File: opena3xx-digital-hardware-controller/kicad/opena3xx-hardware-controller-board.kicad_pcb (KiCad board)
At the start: 2 copper layers, 156.3 x 80.6 mm, 52 parts, among them J1 Conn_02x01, J2 Conn_02x01, J3 Conn_02x01, J4 Conn_02x01, J5 Raspberry_Pi_Zero, SW1 SW_MEC_5E, U1 MCP23017_SO, U2 MCP23017_SO, U3 MCP23017_SO, U4 MCP23017_SO, U5 MCP23017_SO, U6 MCP23017_SO, U7 MCP23017_SO, U8 MCP23017_SO

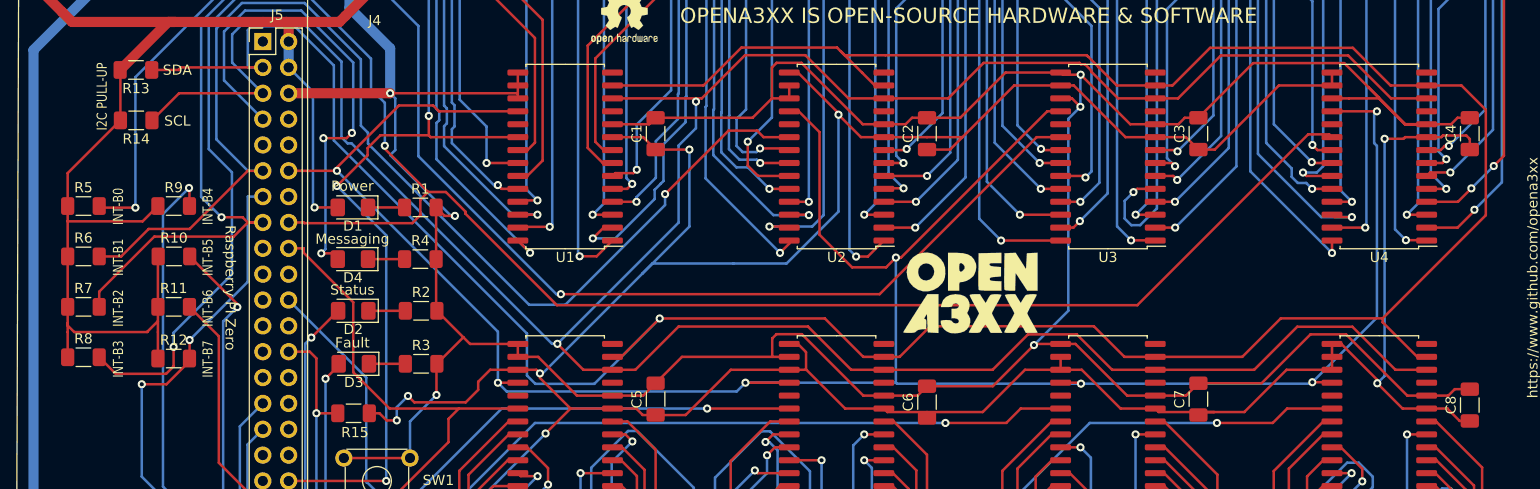
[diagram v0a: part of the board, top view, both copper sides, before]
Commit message: Changed text from Messaging to Signal in Top Mask
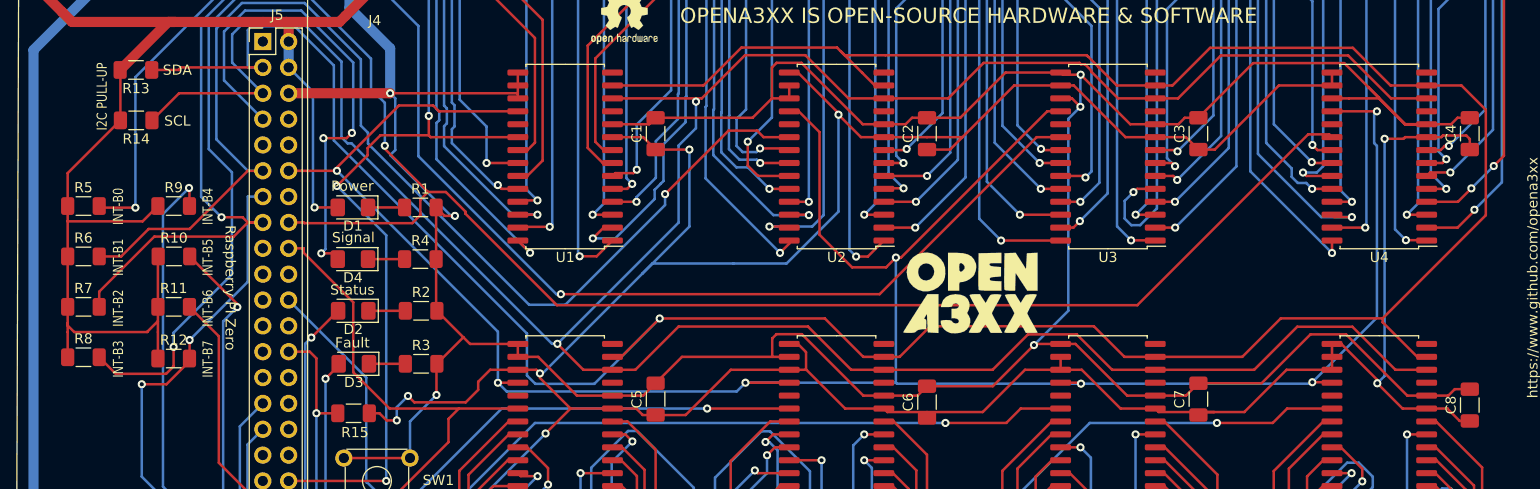
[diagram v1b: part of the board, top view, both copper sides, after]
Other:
- board text added: "Signal"
- board text removed: "Messaging"

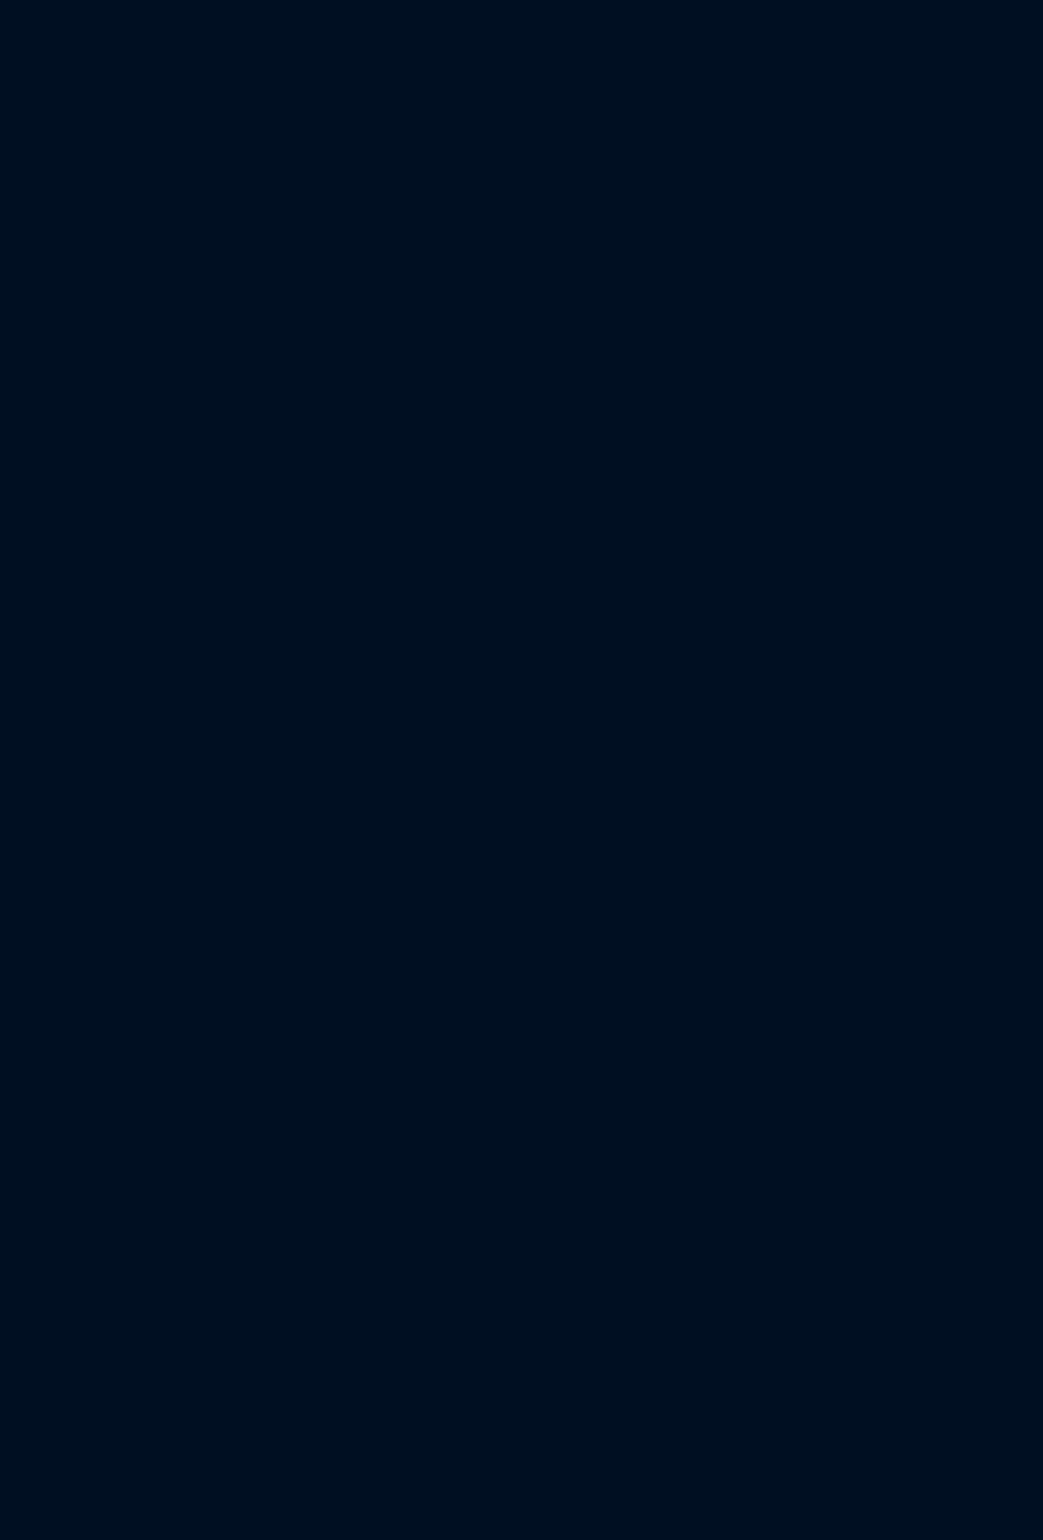
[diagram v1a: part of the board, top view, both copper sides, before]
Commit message: Created mcdu project in Kicad
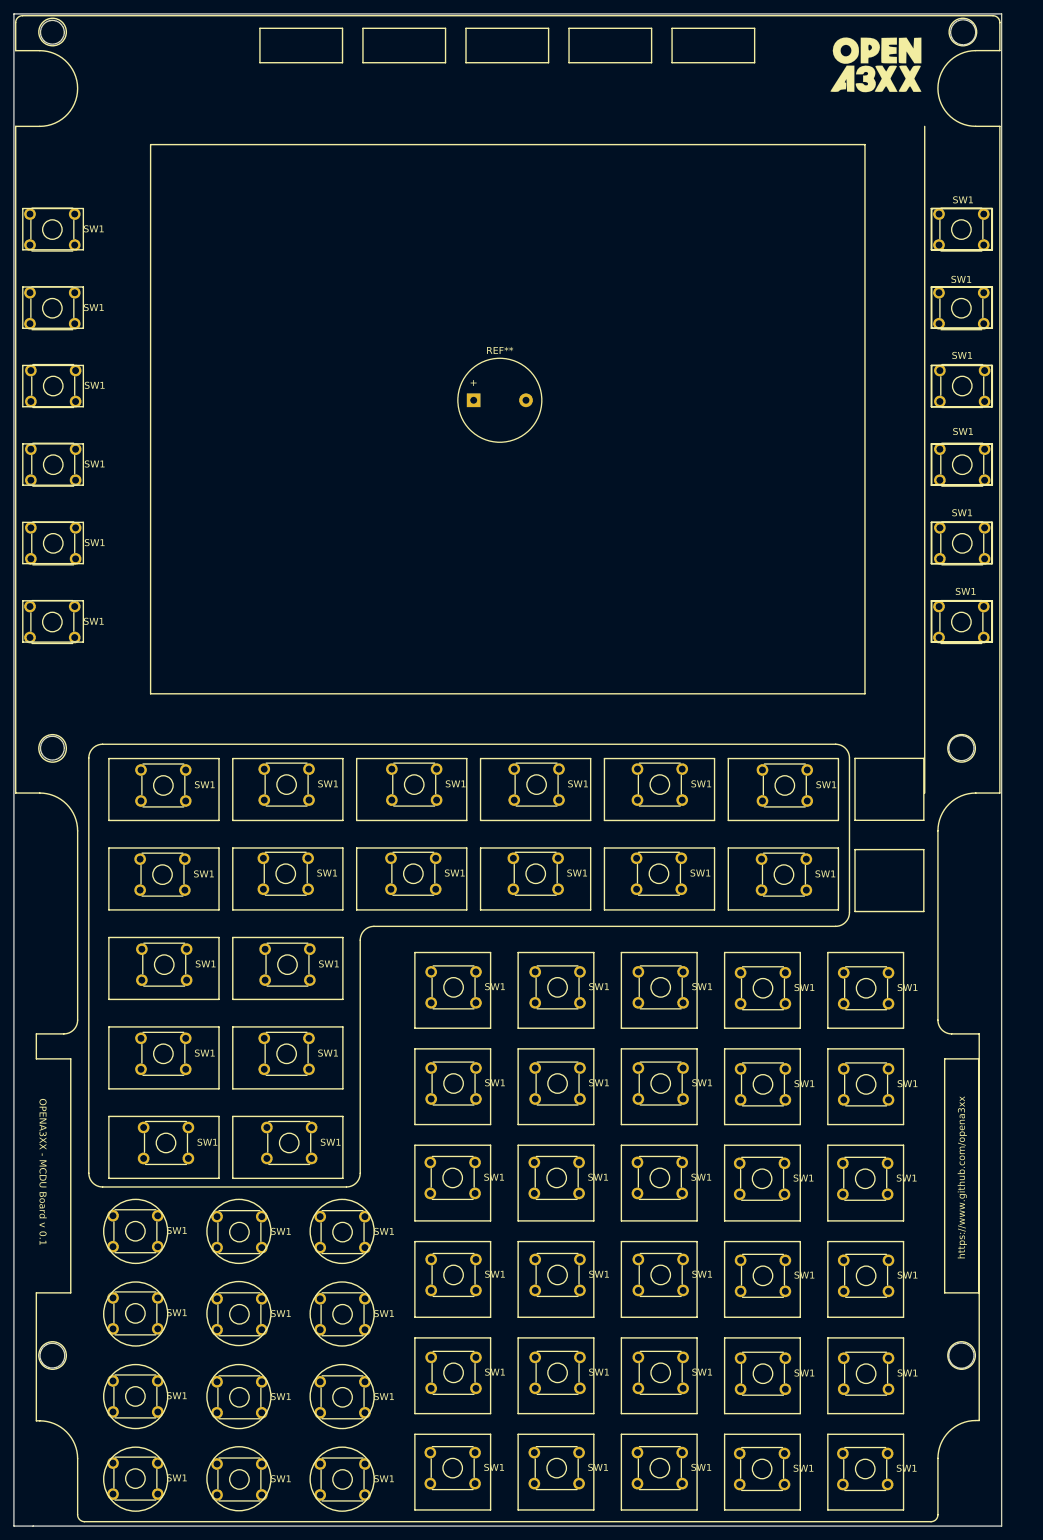
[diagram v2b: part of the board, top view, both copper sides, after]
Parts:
- added G***: LOGO, openaa3xx:logo_180x112, F.Cu at (-34.2, -0.78)
- added REF**: Buzzer_12x9.5RM7.6, Buzzer_Beeper:Buzzer_12x9.5RM7.6, F.Cu at (-92.4, 47.9)
- added SW1: SW_MEC_5E, Button_Switch_THT:SW_TH_Tactile_Omron_B3F-10xx, F.Cu at (-122.5, 153.6)
- added SW1: SW_MEC_5E, Button_Switch_THT:SW_TH_Tactile_Omron_B3F-10xx, F.Cu at (-68.6, 101.5)
- added SW1: SW_MEC_5E, Button_Switch_THT:SW_TH_Tactile_Omron_B3F-10xx, F.Cu at (-86.6, 114.5)
- added SW1: SW_MEC_5E, Button_Switch_THT:SW_TH_Tactile_Omron_B3F-10xx, F.Cu at (-86.5, 101.5)
- added SW1: SW_MEC_5E, Button_Switch_THT:SW_TH_Tactile_Omron_B3F-10xx, F.Cu at (-104.4, 114.5)
- added SW1: SW_MEC_5E, Button_Switch_THT:SW_TH_Tactile_Omron_B3F-10xx, F.Cu at (-104.3, 101.5)
- added SW1: SW_MEC_5E, Button_Switch_THT:SW_TH_Tactile_Omron_B3F-10xx, F.Cu at (-123.0, 114.5)
- added SW1: SW_MEC_5E, Button_Switch_THT:SW_TH_Tactile_Omron_B3F-10xx, F.Cu at (-122.8, 101.5)
- added SW1: SW_MEC_5E, Button_Switch_THT:SW_TH_Tactile_Omron_B3F-10xx, F.Cu at (-140.9, 114.6)
- added SW1: SW_MEC_5E, Button_Switch_THT:SW_TH_Tactile_Omron_B3F-10xx, F.Cu at (-140.7, 101.6)
- added SW1: SW_MEC_5E, Button_Switch_THT:SW_TH_Tactile_Omron_B3F-10xx, F.Cu at (-98.7, 200.8)
- added SW1: SW_MEC_5E, Button_Switch_THT:SW_TH_Tactile_Omron_B3F-10xx, F.Cu at (-140.4, 153.6)
- added SW1: SW_MEC_5E, Button_Switch_THT:SW_TH_Tactile_Omron_B3F-10xx, F.Cu at (-53.7, 201.0)
- added SW1: SW_MEC_5E, Button_Switch_THT:SW_TH_Tactile_Omron_B3F-10xx, F.Cu at (-83.6, 200.8)
- added SW1: SW_MEC_5E, Button_Switch_THT:SW_TH_Tactile_Omron_B3F-10xx, F.Cu at (-38.8, 201.0)
- added SW1: SW_MEC_5E, Button_Switch_THT:SW_TH_Tactile_Omron_B3F-10xx, F.Cu at (-68.6, 200.8)
- added SW1: SW_MEC_5E, Button_Switch_THT:SW_TH_Tactile_Omron_B3F-10xx, F.Cu at (-98.6, 187.0)
- added SW1: SW_MEC_5E, Button_Switch_THT:SW_TH_Tactile_Omron_B3F-10xx, F.Cu at (-53.6, 187.1)
- added SW1: SW_MEC_5E, Button_Switch_THT:SW_TH_Tactile_Omron_B3F-10xx, F.Cu at (-83.5, 187.0)
- added SW1: SW_MEC_5E, Button_Switch_THT:SW_TH_Tactile_Omron_B3F-10xx, F.Cu at (-38.6, 187.1)
- added SW1: SW_MEC_5E, Button_Switch_THT:SW_TH_Tactile_Omron_B3F-10xx, F.Cu at (-68.5, 187.0)
- added SW1: SW_MEC_5E, Button_Switch_THT:SW_TH_Tactile_Omron_B3F-10xx, F.Cu at (-98.6, 172.8)
- added SW1: SW_MEC_5E, Button_Switch_THT:SW_TH_Tactile_Omron_B3F-10xx, F.Cu at (-122.8, 140.6)
- added SW1: SW_MEC_5E, Button_Switch_THT:SW_TH_Tactile_Omron_B3F-10xx, F.Cu at (-53.6, 172.9)
- added SW1: SW_MEC_5E, Button_Switch_THT:SW_TH_Tactile_Omron_B3F-10xx, F.Cu at (-83.5, 172.8)
- added SW1: SW_MEC_5E, Button_Switch_THT:SW_TH_Tactile_Omron_B3F-10xx, F.Cu at (-38.6, 172.9)
- added SW1: SW_MEC_5E, Button_Switch_THT:SW_TH_Tactile_Omron_B3F-10xx, F.Cu at (-68.5, 172.8)
- added SW1: SW_MEC_5E, Button_Switch_THT:SW_TH_Tactile_Omron_B3F-10xx, F.Cu at (-98.7, 158.7)
- added SW1: SW_MEC_5E, Button_Switch_THT:SW_TH_Tactile_Omron_B3F-10xx, F.Cu at (-53.7, 158.8)
- added SW1: SW_MEC_5E, Button_Switch_THT:SW_TH_Tactile_Omron_B3F-10xx, F.Cu at (-83.6, 158.7)
- added SW1: SW_MEC_5E, Button_Switch_THT:SW_TH_Tactile_Omron_B3F-10xx, F.Cu at (-38.8, 158.8)
- added SW1: SW_MEC_5E, Button_Switch_THT:SW_TH_Tactile_Omron_B3F-10xx, F.Cu at (-68.6, 158.7)
- added SW1: SW_MEC_5E, Button_Switch_THT:SW_TH_Tactile_Omron_B3F-10xx, F.Cu at (-98.6, 144.9)
- added SW1: SW_MEC_5E, Button_Switch_THT:SW_TH_Tactile_Omron_B3F-10xx, F.Cu at (-122.7, 127.7)
- added SW1: SW_MEC_5E, Button_Switch_THT:SW_TH_Tactile_Omron_B3F-10xx, F.Cu at (-53.6, 145.1)
- added SW1: SW_MEC_5E, Button_Switch_THT:SW_TH_Tactile_Omron_B3F-10xx, F.Cu at (-83.5, 144.9)
- added SW1: SW_MEC_5E, Button_Switch_THT:SW_TH_Tactile_Omron_B3F-10xx, F.Cu at (-38.6, 145.1)
- added SW1: SW_MEC_5E, Button_Switch_THT:SW_TH_Tactile_Omron_B3F-10xx, F.Cu at (-68.5, 144.9)
- added SW1: SW_MEC_5E, Button_Switch_THT:SW_TH_Tactile_Omron_B3F-10xx, F.Cu at (-38.6, 131.1)
- added SW1: SW_MEC_5E, Button_Switch_THT:SW_TH_Tactile_Omron_B3F-10xx, F.Cu at (-53.6, 131.1)
- added SW1: SW_MEC_5E, Button_Switch_THT:SW_TH_Tactile_Omron_B3F-10xx, F.Cu at (-68.5, 131.0)
- added SW1: SW_MEC_5E, Button_Switch_THT:SW_TH_Tactile_Omron_B3F-10xx, F.Cu at (-83.5, 131.0)
- added SW1: SW_MEC_5E, Button_Switch_THT:SW_TH_Tactile_Omron_B3F-10xx, F.Cu at (-98.6, 131.0)
- added SW1: SW_MEC_5E, Button_Switch_THT:SW_TH_Tactile_Omron_B3F-10xx, F.Cu at (-114.7, 202.5)
- added SW1: SW_MEC_5E, Button_Switch_THT:SW_TH_Tactile_Omron_B3F-10xx, F.Cu at (-140.7, 140.6)
- added SW1: SW_MEC_5E, Button_Switch_THT:SW_TH_Tactile_Omron_B3F-10xx, F.Cu at (-144.8, 202.3)
- added SW1: SW_MEC_5E, Button_Switch_THT:SW_TH_Tactile_Omron_B3F-10xx, F.Cu at (-129.7, 202.5)
- added SW1: SW_MEC_5E, Button_Switch_THT:SW_TH_Tactile_Omron_B3F-10xx, F.Cu at (-114.7, 190.5)
- added SW1: SW_MEC_5E, Button_Switch_THT:SW_TH_Tactile_Omron_B3F-10xx, F.Cu at (-144.8, 190.4)
- added SW1: SW_MEC_5E, Button_Switch_THT:SW_TH_Tactile_Omron_B3F-10xx, F.Cu at (-129.7, 190.5)
- added SW1: SW_MEC_5E, Button_Switch_THT:SW_TH_Tactile_Omron_B3F-10xx, F.Cu at (-114.7, 178.5)
- added SW1: SW_MEC_5E, Button_Switch_THT:SW_TH_Tactile_Omron_B3F-10xx, F.Cu at (-144.8, 178.3)
- added SW1: SW_MEC_5E, Button_Switch_THT:SW_TH_Tactile_Omron_B3F-10xx, F.Cu at (-129.7, 178.5)
- added SW1: SW_MEC_5E, Button_Switch_THT:SW_TH_Tactile_Omron_B3F-10xx, F.Cu at (-114.7, 166.5)
- added SW1: SW_MEC_5E, Button_Switch_THT:SW_TH_Tactile_Omron_B3F-10xx, F.Cu at (-24.7, 43.6)
- added SW1: SW_MEC_5E, Button_Switch_THT:SW_TH_Tactile_Omron_B3F-10xx, F.Cu at (-140.6, 127.7)
- added SW1: SW_MEC_5E, Button_Switch_THT:SW_TH_Tactile_Omron_B3F-10xx, F.Cu at (-24.8, 20.9)
- added SW1: SW_MEC_5E, Button_Switch_THT:SW_TH_Tactile_Omron_B3F-10xx, F.Cu at (-24.8, 77.9)
- added SW1: SW_MEC_5E, Button_Switch_THT:SW_TH_Tactile_Omron_B3F-10xx, F.Cu at (-24.7, 66.5)
- added SW1: SW_MEC_5E, Button_Switch_THT:SW_TH_Tactile_Omron_B3F-10xx, F.Cu at (-24.7, 55.0)
- added SW1: SW_MEC_5E, Button_Switch_THT:SW_TH_Tactile_Omron_B3F-10xx, F.Cu at (-24.8, 32.3)
- added SW1: SW_MEC_5E, Button_Switch_THT:SW_TH_Tactile_Omron_B3F-10xx, F.Cu at (-129.7, 166.5)
- added SW1: SW_MEC_5E, Button_Switch_THT:SW_TH_Tactile_Omron_B3F-10xx, F.Cu at (-144.8, 166.4)
- added SW1: SW_MEC_5E, Button_Switch_THT:SW_TH_Tactile_Omron_B3F-10xx, F.Cu at (-156.9, 77.9)
- added SW1: SW_MEC_5E, Button_Switch_THT:SW_TH_Tactile_Omron_B3F-10xx, F.Cu at (-156.7, 66.5)
- added SW1: SW_MEC_5E, Button_Switch_THT:SW_TH_Tactile_Omron_B3F-10xx, F.Cu at (-156.7, 55.0)
- added SW1: SW_MEC_5E, Button_Switch_THT:SW_TH_Tactile_Omron_B3F-10xx, F.Cu at (-50.6, 114.6)
- added SW1: SW_MEC_5E, Button_Switch_THT:SW_TH_Tactile_Omron_B3F-10xx, F.Cu at (-156.7, 43.6)
- added SW1: SW_MEC_5E, Button_Switch_THT:SW_TH_Tactile_Omron_B3F-10xx, F.Cu at (-156.9, 32.3)
- added SW1: SW_MEC_5E, Button_Switch_THT:SW_TH_Tactile_Omron_B3F-10xx, F.Cu at (-156.9, 20.9)
- added SW1: SW_MEC_5E, Button_Switch_THT:SW_TH_Tactile_Omron_B3F-10xx, F.Cu at (-50.4, 101.6)
- added SW1: SW_MEC_5E, Button_Switch_THT:SW_TH_Tactile_Omron_B3F-10xx, F.Cu at (-68.7, 114.5)
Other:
- board size 156.3 x 80.6 mm -> 374.5 x 219.7 mm
- board text added: "OPENA3XX - MCDU Board v 0.1"

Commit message: WIP Schematic & PCB for the MCDU Added custom Kicad Packages for the Tactile Switchs (LED EMBEDDED)
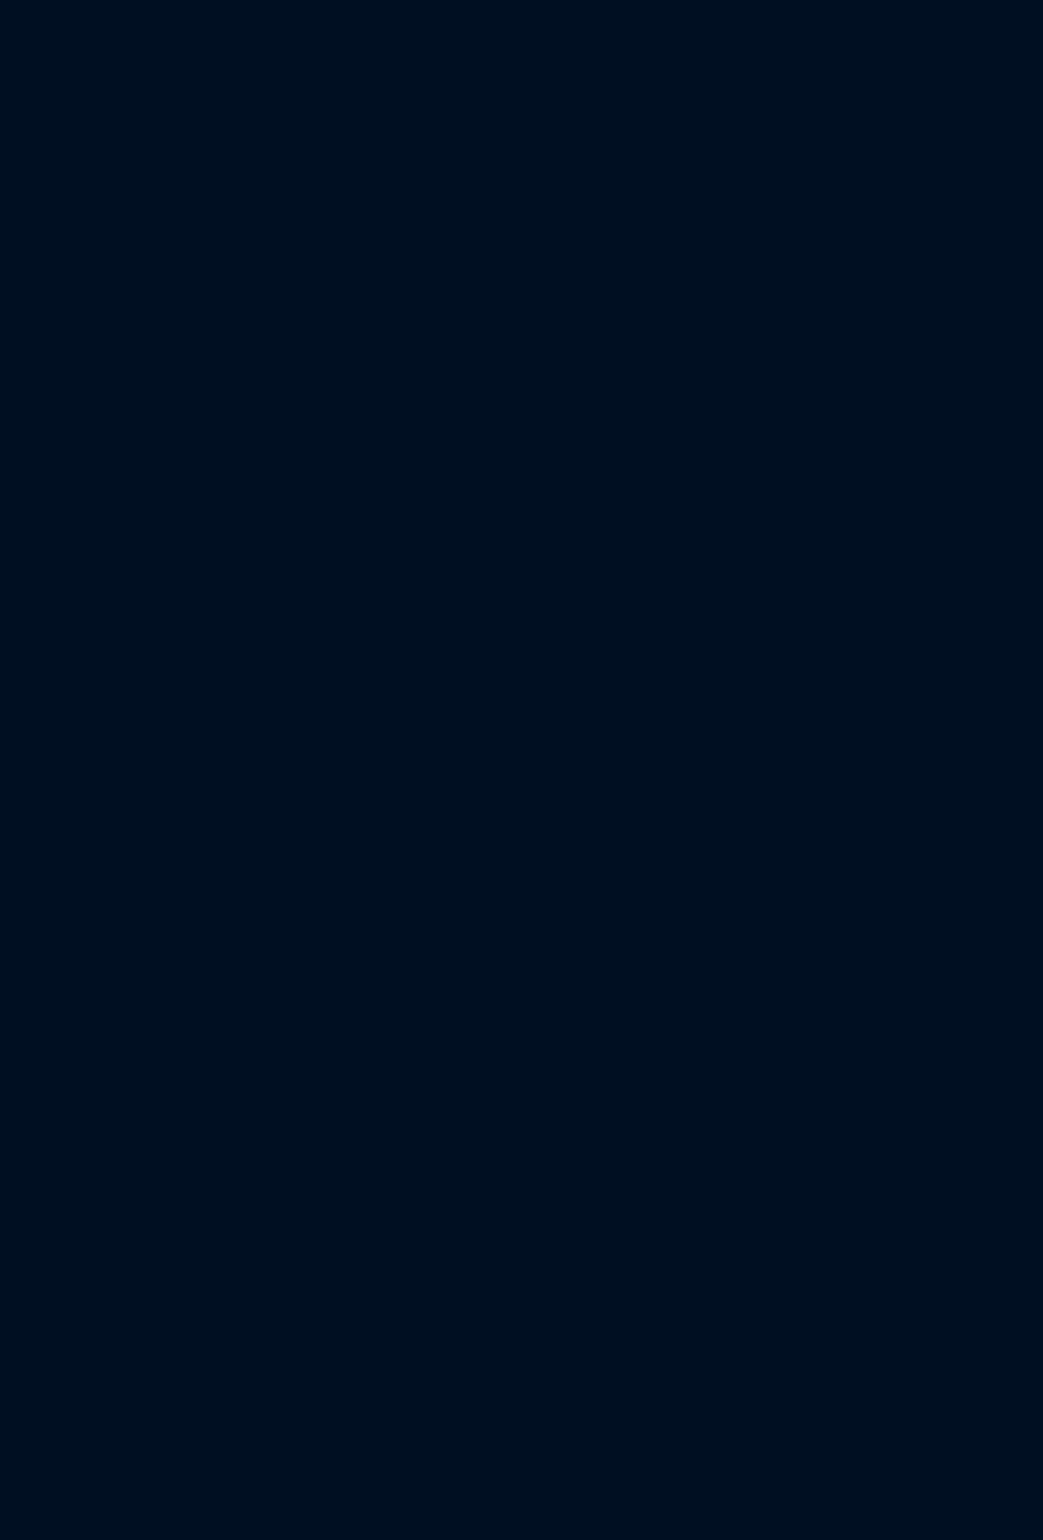
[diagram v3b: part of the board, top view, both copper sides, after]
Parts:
- removed the G*** at (-34.2, -0.78)
- removed the REF** at (-92.4, 47.9)
- removed the SW1 at (-122.5, 153.6)
- removed the SW1 at (-68.6, 101.5)
- removed the SW1 at (-86.6, 114.5)
- removed the SW1 at (-86.5, 101.5)
- removed the SW1 at (-104.4, 114.5)
- removed the SW1 at (-104.3, 101.5)
- removed the SW1 at (-123.0, 114.5)
- removed the SW1 at (-122.8, 101.5)
- removed the SW1 at (-140.9, 114.6)
- removed the SW1 at (-140.7, 101.6)
- removed the SW1 at (-98.7, 200.8)
- removed the SW1 at (-140.4, 153.6)
- removed the SW1 at (-53.7, 201.0)
- removed the SW1 at (-83.6, 200.8)
- removed the SW1 at (-38.8, 201.0)
- removed the SW1 at (-68.6, 200.8)
- removed the SW1 at (-98.6, 187.0)
- removed the SW1 at (-53.6, 187.1)
- removed the SW1 at (-83.5, 187.0)
- removed the SW1 at (-38.6, 187.1)
- removed the SW1 at (-68.5, 187.0)
- removed the SW1 at (-98.6, 172.8)
- removed the SW1 at (-122.8, 140.6)
- removed the SW1 at (-53.6, 172.9)
- removed the SW1 at (-83.5, 172.8)
- removed the SW1 at (-38.6, 172.9)
- removed the SW1 at (-68.5, 172.8)
- removed the SW1 at (-98.7, 158.7)
- removed the SW1 at (-53.7, 158.8)
- removed the SW1 at (-83.6, 158.7)
- removed the SW1 at (-38.8, 158.8)
- removed the SW1 at (-68.6, 158.7)
- removed the SW1 at (-98.6, 144.9)
- removed the SW1 at (-122.7, 127.7)
- removed the SW1 at (-53.6, 145.1)
- removed the SW1 at (-83.5, 144.9)
- removed the SW1 at (-38.6, 145.1)
- removed the SW1 at (-68.5, 144.9)
- removed the SW1 at (-38.6, 131.1)
- removed the SW1 at (-53.6, 131.1)
- removed the SW1 at (-68.5, 131.0)
- removed the SW1 at (-83.5, 131.0)
- removed the SW1 at (-98.6, 131.0)
- removed the SW1 at (-114.7, 202.5)
- removed the SW1 at (-140.7, 140.6)
- removed the SW1 at (-144.8, 202.3)
- removed the SW1 at (-129.7, 202.5)
- removed the SW1 at (-114.7, 190.5)
- removed the SW1 at (-144.8, 190.4)
- removed the SW1 at (-129.7, 190.5)
- removed the SW1 at (-114.7, 178.5)
- removed the SW1 at (-144.8, 178.3)
- removed the SW1 at (-129.7, 178.5)
- removed the SW1 at (-114.7, 166.5)
- removed the SW1 at (-24.7, 43.6)
- removed the SW1 at (-140.6, 127.7)
- removed the SW1 at (-24.8, 20.9)
- removed the SW1 at (-24.8, 77.9)
- removed the SW1 at (-24.7, 66.5)
- removed the SW1 at (-24.7, 55.0)
- removed the SW1 at (-24.8, 32.3)
- removed the SW1 at (-129.7, 166.5)
- removed the SW1 at (-144.8, 166.4)
- removed the SW1 at (-156.9, 77.9)
- removed the SW1 at (-156.7, 66.5)
- removed the SW1 at (-156.7, 55.0)
- removed the SW1 at (-50.6, 114.6)
- removed the SW1 at (-156.7, 43.6)
- removed the SW1 at (-156.9, 32.3)
- removed the SW1 at (-156.9, 20.9)
- removed the SW1 at (-50.4, 101.6)
- removed the SW1 at (-68.7, 114.5)
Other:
- board size 374.5 x 219.7 mm -> 156.3 x 80.6 mm
- board text removed: "OPENA3XX - MCDU Board v 0.1"
